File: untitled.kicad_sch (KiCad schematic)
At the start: 21 parts, among them J3 Conn_01x05_Pin, J4 Conn_01x05_Pin, J5 Conn_01x05_Pin, J6 Conn_01x05_Pin, J7 Conn_01x04_Pin, J8 Conn_01x02_Socket, J9 Conn_01x02_Pin, U3 ESP32-WROOM-32, U4 MPU-6500, U5 TPS62933DRLR

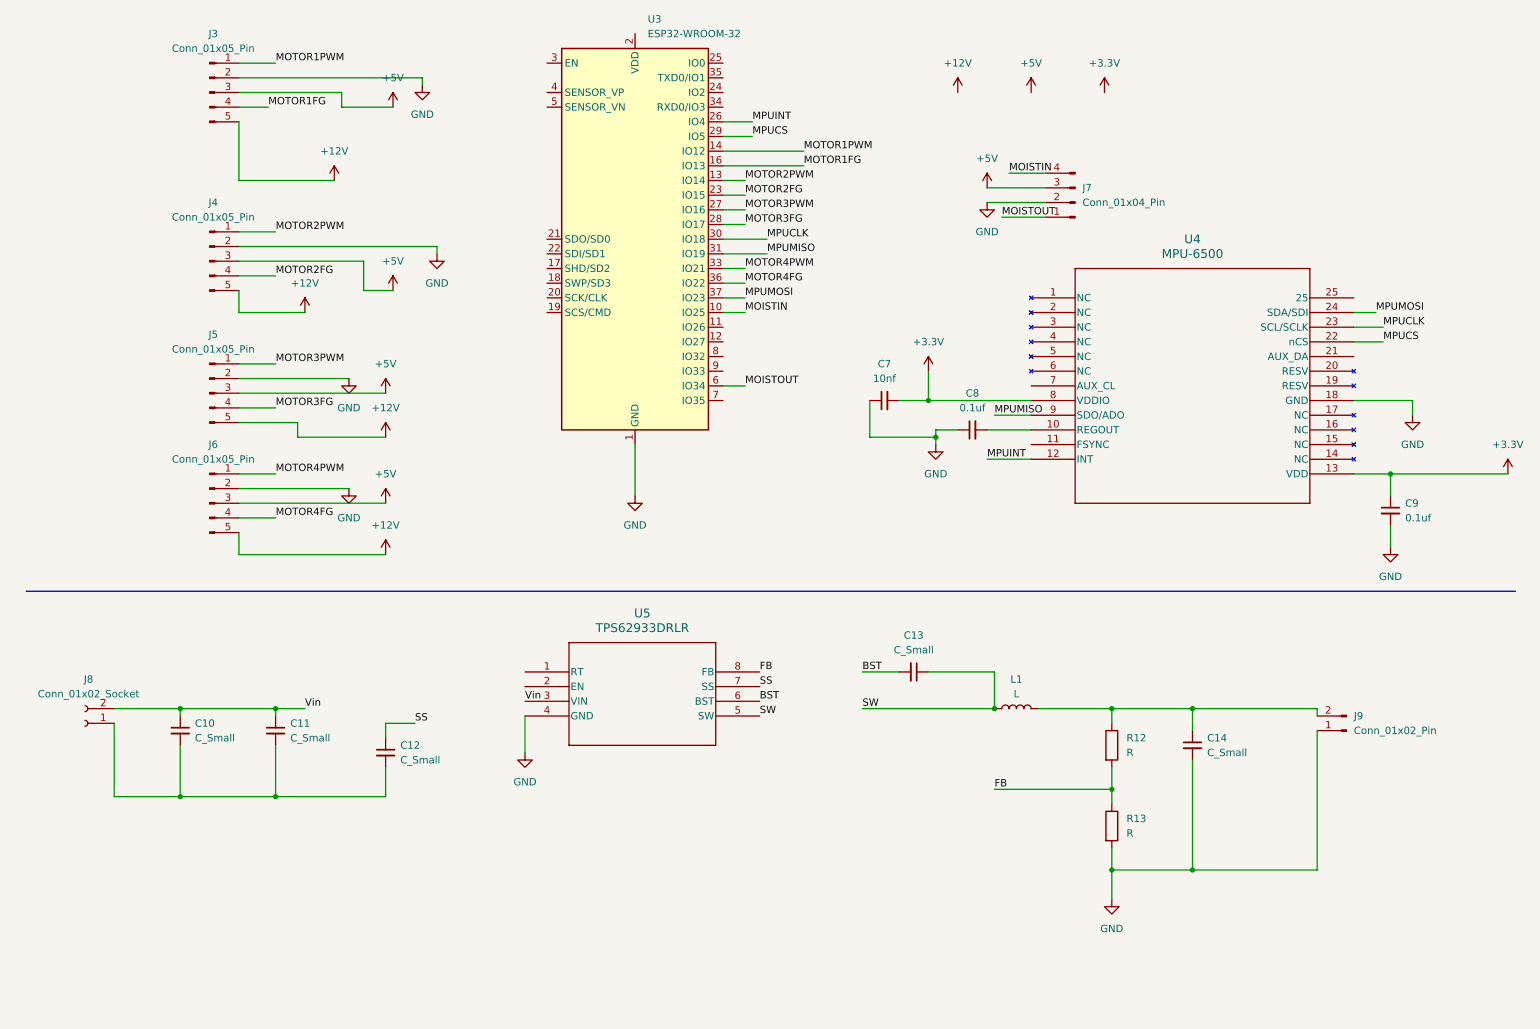
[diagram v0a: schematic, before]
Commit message: Added soil moisture sensor
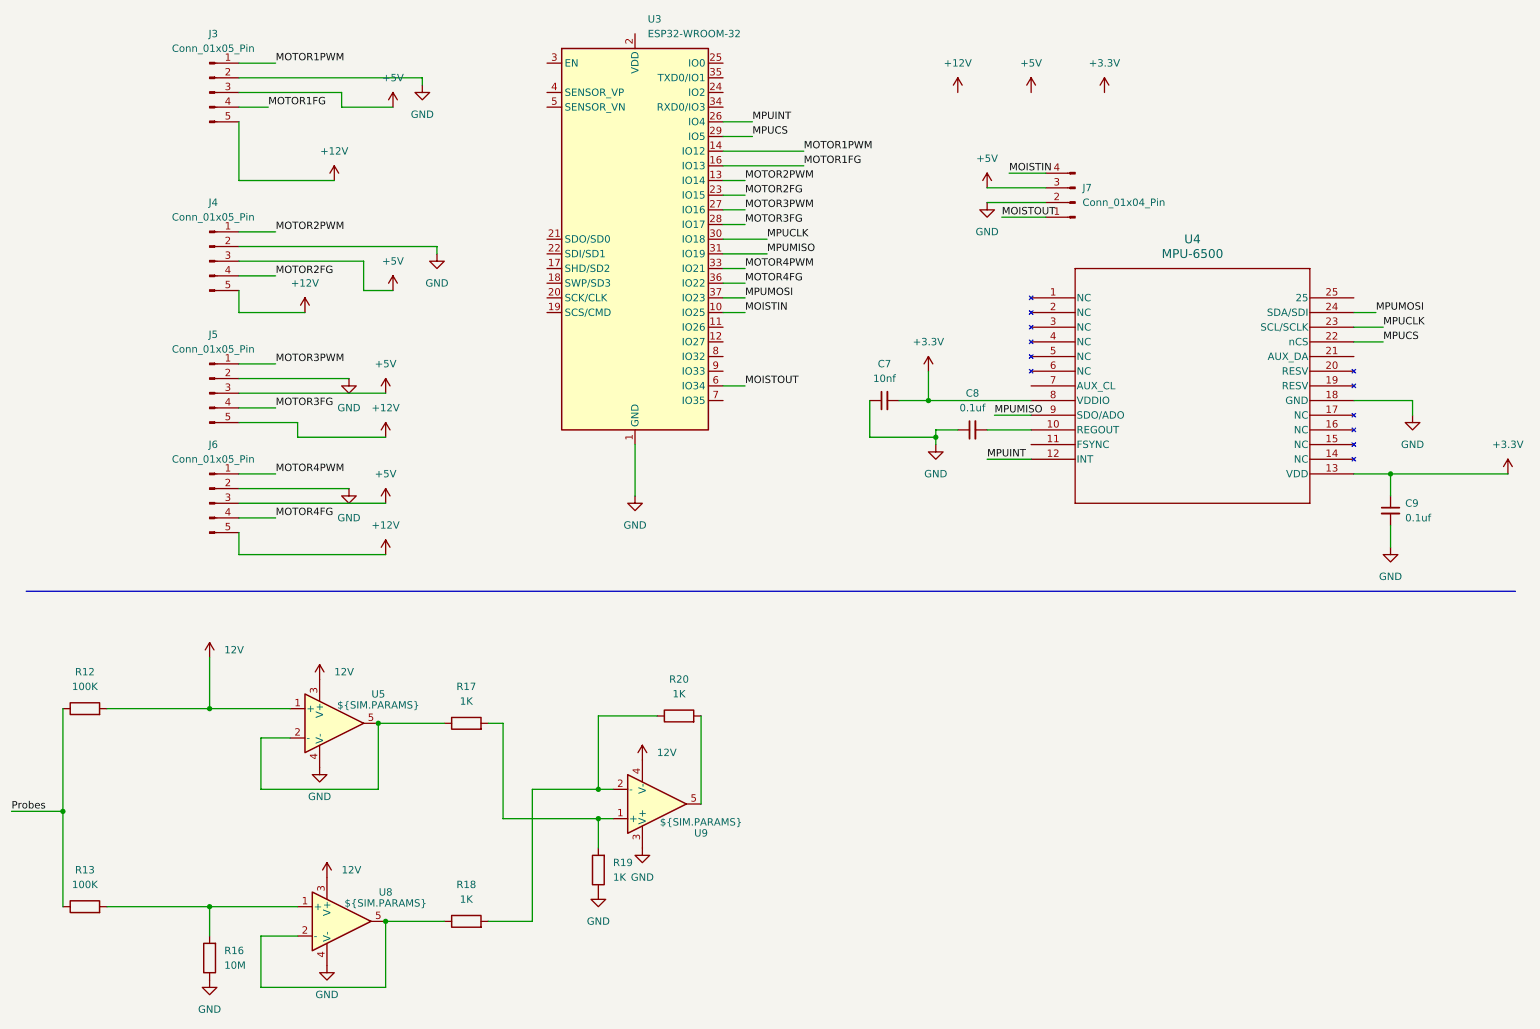
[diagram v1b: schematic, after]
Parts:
- removed C10, C11, C12, C13, C14: C_Small, symbol Device:C_Small
- removed J8: Conn_01x02_Socket, symbol Connector:Conn_01x02_Socket
- removed J9: Conn_01x02_Pin, symbol Connector:Conn_01x02_Pin
- removed L1: L, symbol Device:L
- removed U5: TPS62933DRLR, SOT-5X3-8_DRL_TEX, symbol TPS62933DRLR:TPS62933DRLR
- added R16: 10M, symbol Device:R
- added R17, R18, R19, R20: 1K, symbol Device:R
- added U5, U8, U9: ${SIM.PARAMS}, symbol Simulation_SPICE:OPAMP
- R12, R13: value R -> 100K
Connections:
- net GND: now also R16.1, R19.1, U5.4 (V-), U8.4 (V-), U9.3 (V+); no longer R13.2
- net Probes: now reaches R12.1
- net Probes: now also R13.1
- net FB renamed 12V
- net 12V: now also U5.1 (+), U5.3 (V+), U8.3 (V+), U9.4 (V-); no longer R13.1
- new net: R13.2, R16.2, U8.1 (+)
- new net: R18.1, U8.2 (-), U8.5
- new net: R17.2, R19.2, U9.1 (+)
- new net: R18.2, R20.1, U9.2 (-)
- new net: R17.1, U5.2 (-), U5.5
- new net: R20.2, U9.5
